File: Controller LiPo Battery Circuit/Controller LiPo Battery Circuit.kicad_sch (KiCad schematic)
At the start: 39 parts, among them CN1 USBA_FEMALE, J1 Jack-DC, Q1 MMUN2133LT1G, Q2 BC548, SW1 ROTARY SW, U1 TPS61090RSAR, U2 MCP73831T-2ACI/OT, X1 TERMBLOCK_1X2, X2 microUSB

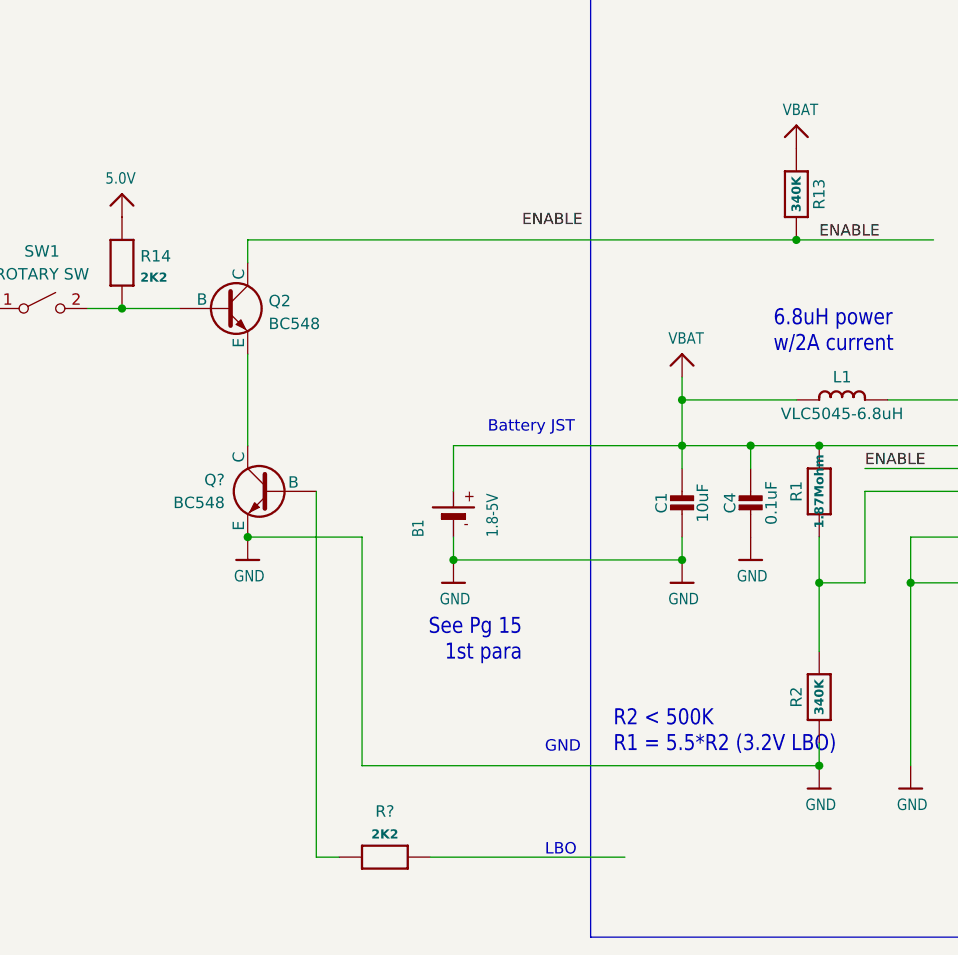
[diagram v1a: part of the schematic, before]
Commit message: Just connected LBO to Enable
Decided that we didn't need transistor control of the LBO to Enable line
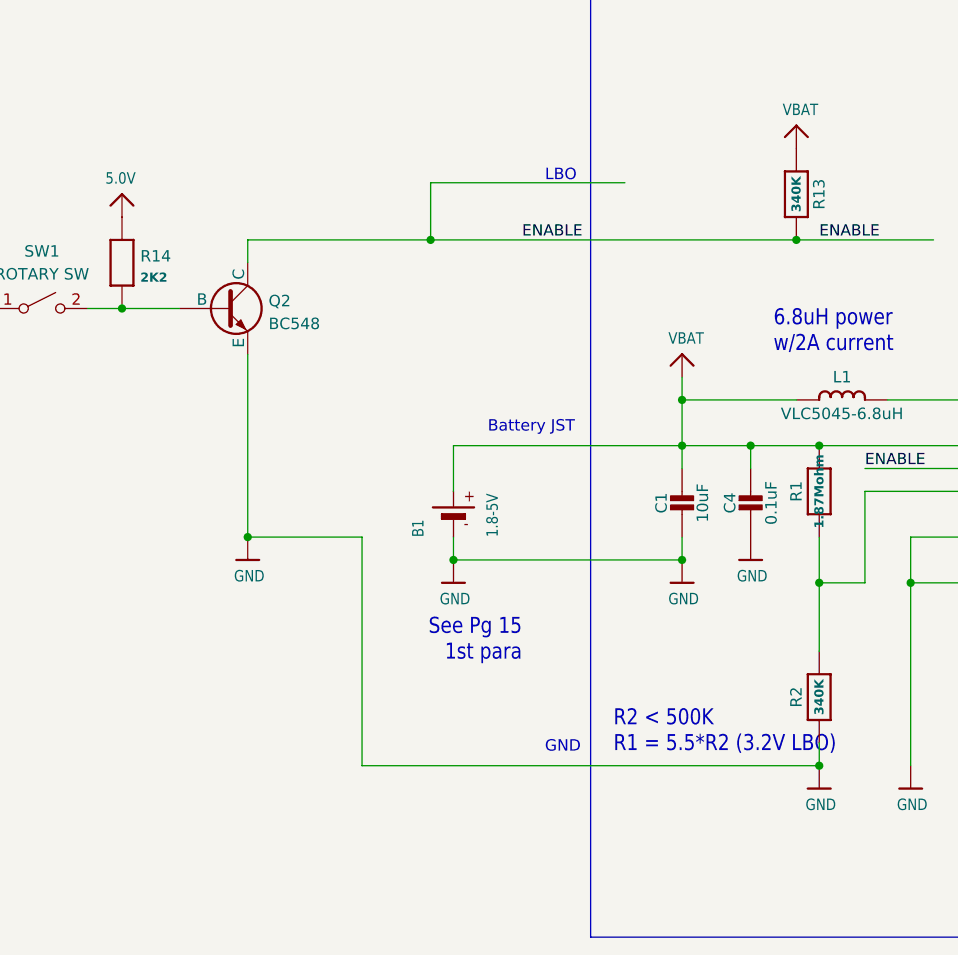
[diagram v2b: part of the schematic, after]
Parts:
- removed Q?: BC548, Package_TO_SOT_THT:TO-92_Inline, symbol Transistor_BJT:BC548
- removed R?: 2K2, Controller LiPo Battery Circuit:0603-MINI, symbol Controller LiPo Battery Circuit-eagle-import:RESISTOR0603MINI
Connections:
- net GND: now also Q2.3 (E)
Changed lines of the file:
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@@
   (junction (at 214.63 111.76) (diameter 0) (color 0 0 0 0)
   )
+  (junction (at 100.33 109.22) (diameter 0) (color 0 0 0 0)
+  )
+  (junction (at 135.89 132.08) (diameter 0) (color 0 0 0 0)
+  )
+  (junction (at 143.51 132.08) (diameter 0) (color 0 0 0 0)
+  )
+  (junction (at 140.97 109.22) (diameter 0) (color 0 0 0 0)
+  )
+  (junction (at 191.77 147.32) (diameter 0) (color 0 0 0 0)
+  )
+  (junction (at 214.63 127) (diameter 0) (color 0 0 0 0)
+  )
+  (junction (at 143.51 147.32) (diameter 0) (color 0 0 0 0)
+  )
+  (junction (at 196.85 127) (diameter 0) (color 0 0 0 0)
+  )
+  (junction (at 260.35 66.04) (diameter 0) (color 0 0 0 0)
+  )
+  (junction (at 270.51 124.46) (diameter 0) (color 0 0 0 0)
+  )
+  (junction (at 270.51 137.16) (diameter 0) (color 0 0 0 0)
+  )
+  (junction (at 336.55 88.9) (diameter 0) (color 0 0 0 0)
+  )
+  (junction (at 267.97 66.04) (diameter 0) (color 0 0 0 0)
+  )
+  (junction (at 143.51 167.64) (diameter 0) (color 0 0 0 0)
+  )
+  (junction (at 273.05 143.51) (diameter 0) (color 0 0 0 0)
+  )
+  (junction (at 128.27 144.78) (diameter 0) (color 0 0 0 0)
+  )
+  (junction (at 191.77 127) (diameter 0) (color 0 0 0 0)
+  )
   (junction (at 80.01 142.24) (diameter 0) (color 0 0 0 0)
   )
-  (junction (at 135.89 132.08) (diameter 0) (color 0 0 0 0)
-  )
-  (junction (at 143.51 132.08) (diameter 0) (color 0 0 0 0)
-  )
-  (junction (at 140.97 109.22) (diameter 0) (color 0 0 0 0)
-  )
-  (junction (at 191.77 147.32) (diameter 0) (color 0 0 0 0)
-  )
-  (junction (at 214.63 127) (diameter 0) (color 0 0 0 0)
-  )
-  (junction (at 143.51 147.32) (diameter 0) (color 0 0 0 0)
-  )
-  (junction (at 196.85 127) (diameter 0) (color 0 0 0 0)
-  )
-  (junction (at 260.35 66.04) (diameter 0) (color 0 0 0 0)
-  )
-  (junction (at 270.51 124.46) (diameter 0) (color 0 0 0 0)
-  )
-  (junction (at 270.51 137.16) (diameter 0) (color 0 0 0 0)
-  )
-  (junction (at 336.55 88.9) (diameter 0) (color 0 0 0 0)
-  )
-  (junction (at 267.97 66.04) (diameter 0) (color 0 0 0 0)
-  )
-  (junction (at 143.51 167.64) (diameter 0) (color 0 0 0 0)
-  )
-  (junction (at 273.05 143.51) (diameter 0) (color 0 0 0 0)
-  )
-  (junction (at 128.27 144.78) (diameter 0) (color 0 0 0 0)
-  )
-  (junction (at 191.77 127) (diameter 0) (color 0 0 0 0)
-  )
   (junction (at 273.05 120.65) (diameter 0) (color 0 0 0 0)
   )
@@
     (stroke (width 0) (type default) (color 0 0 0 0))
   )
+  (wire (pts (xy 100.33 109.22) (xy 140.97 109.22))
+    (stroke (width 0) (type default) (color 0 0 0 0))
+  )
   (wire (pts (xy 102.87 144.78) (xy 128.27 144.78))
     (stroke (width 0) (type default) (color 0 0 0 0))
@@
     (stroke (width 0) (type default) (color 0 0 0 0))
   )
-  (wire (pts (xy 80.01 121.92) (xy 80.01 132.08))
+  (wire (pts (xy 80.01 121.92) (xy 80.01 142.24))
     (stroke (width 0) (type default) (color 0 0 0 0))
   )
@@
     (stroke (width 0) (type default) (color 0 0 0 0))
   )
-  (wire (pts (xy 87.63 137.16) (xy 87.63 177.8))
-    (stroke (width 0) (type default) (color 0 0 0 0))
-  )
   (wire (pts (xy 293.37 78.74) (xy 293.37 71.12))
     (stroke (width 0) (type default) (color 0 0 0 0))
   )
-  (wire (pts (xy 80.01 109.22) (xy 140.97 109.22))
+  (wire (pts (xy 80.01 109.22) (xy 100.33 109.22))
     (stroke (width 0) (type default) (color 0 0 0 0))
   )
@@
     (stroke (width 0) (type default) (color 0 0 0 0))
   )
-  (wire (pts (xy 100.33 177.8) (xy 121.92 177.8))
+  (wire (pts (xy 100.33 102.87) (xy 121.92 102.87))
     (stroke (width 0) (type default) (color 0 0 0 0))
   )
@@
     (stroke (width 0) (type default) (color 0 0 0 0))
   )
+  (wire (pts (xy 100.33 102.87) (xy 100.33 109.22))
+    (stroke (width 0) (type default) (color 0 0 0 0))
+  )
   (wire (pts (xy 148.59 147.32) (xy 148.59 137.16))
     (stroke (width 0) (type default) (color 0 0 0 0))
@@
   )
   (wire (pts (xy 321.31 71.12) (xy 323.85 71.12))
-    (stroke (width 0) (type default) (color 0 0 0 0))
-  )
-  (wire (pts (xy 87.63 177.8) (xy 90.17 177.8))
     (stroke (width 0) (type default) (color 0 0 0 0))
   )
@@
     (effects (font (size 1.27 1.27)) (justify left bottom))
   )
-  (text "LBO\n" (at 113.03 177.8 0)
+  (text "LBO\n" (at 113.03 102.87 0)
     (effects (font (size 1.27 1.27)) (justify left bottom))
   )
@@
     (effects (font (size 1.016 1.016)) (justify right bottom))
   )
-  (label "ENABLE" (at 110.49 107.95 0)
+  (label "ENABLE" (at 110.49 109.22 0)
     (effects (font (size 1.2446 1.2446)) (justify left bottom))
   )
@@
     (pin "E")
   )
-  (symbol (lib_id "Transistor_BJT:BC548") (at 82.55 137.16 0) (mirror y) (unit 1)
-    (in_bom yes) (on_board yes) (fields_autoplaced)
-    (property "Reference" "Q?" (id 0) (at 77.47 135.8899 0)
-      (effects (font (size 1.27 1.27)) (justify left))
-    )
-    (property "Value" "BC548" (id 1) (at 77.47 138.4299 0)
-      (effects (font (size 1.27 1.27)) (justify left))
-    )
-    (property "Footprint" "Package_TO_SOT_THT:TO-92_Inline" (id 2) (at 77.47 139.065 0)
-      (effects (font (size 1.27 1.27) italic) (justify left) hide)
-    )
-    (property "Datasheet" "https://www.onsemi.com/pub/Collateral/BC550-D.pdf" (id 3) (at 82.55 137.16 0)
-      (effects (font (size 1.27 1.27)) (justify left) hide)
-    )
-    (pin "1")
-    (pin "2")
-    (pin "3")
-  )
   (symbol (lib_id "Controller LiPo Battery Circuit-eagle-import:VBAT") (at 140.97 96.52 0) (unit 1)
     (in_bom yes) (on_board yes)
@@
     (pin "1")
   )
-  (symbol (lib_id "Controller LiPo Battery Circuit-eagle-import:RESISTOR0603MINI") (at 95.25 177.8 180) (unit 1)
-    (in_bom yes) (on_board yes) (fields_autoplaced)
-    (property "Reference" "R?" (id 0) (at 95.25 172.72 0))
-    (property "Value" "2K2" (id 1) (at 95.25 175.26 0)
-      (effects (font (size 1.016 1.016) bold))
-    )
-    (property "Footprint" "Controller LiPo Battery Circuit:0603-MINI" (id 2) (at 95.25 177.8 0)
-      (effects (font (size 1.27 1.27)) hide)
-    )
-    (property "Datasheet" "" (id 3) (at 95.25 177.8 0)
-      (effects (font (size 1.27 1.27)) hide)
-    )
-    (pin "1")
-    (pin "2")
-  )
   (symbol (lib_id "Controller LiPo Battery Circuit-eagle-import:RESISTOR0805_NOOUTLINE") (at 191.77 142.24 90) (unit 1)
     (in_bom yes) (on_board yes)
@@
       (reference "Q2") (unit 1) (value "BC548") (footprint "Package_TO_SOT_THT:TO-92_Inline")
     )
-    (path "/2c106d57-d126-491f-b8e5-3d7b48ca676e"
-      (reference "Q?") (unit 1) (value "BC548") (footprint "Package_TO_SOT_THT:TO-92_Inline")
-    )
     (path "/adda07ce-daac-4e4e-9d52-415971c89ae0"
       (reference "R1") (unit 1) (value "1.87Mohm") (footprint "Controller LiPo Battery Circuit:0805-NO")
@@
       (reference "R20") (unit 1) (value "1K") (footprint "Controller LiPo Battery Circuit:0805-NO")
     )
-    (path "/d76d002d-79a6-493d-beee-cfd6c20e9189"
-      (reference "R?") (unit 1) (value "2K2") (footprint "Controller LiPo Battery Circuit:0603-MINI")
-    )
     (path "/1815e0a6-d6ea-443e-92b7-f4945f548a6a"

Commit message: Starting to create PCB
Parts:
- removed X2: microUSB, Controller LiPo Battery Circuit:4UCONN_20329, symbol Controller LiPo Battery Circuit-eagle-import:USBMICRO_20329
- C5: symbol Controller LiPo Battery Circuit-eagle-import:CAP_TANTALUMB/3528_REFLOW -> Controller LiPo Battery Circuit-eagle-import:CAP_TANTALUMB/3528_REFLOW
- J1: symbol Connector:Jack-DC -> Connector:Conn_01x02_Pin
- U2: symbol Controller LiPo Battery Circuit-eagle-import:MCP73831/2 -> Controller LiPo Battery Circuit-eagle-import:MCP73831/2
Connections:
- net 5.0V is gone; now on net +5V: C2.1, C5.+, CN1.VBUS, JP1.6, PWR0.A, R11.2, R14.2, R3.2, R9.2, U1.1 (VOUT), U1.15 (VOUT), U1.16 (VOUT), X1.2
- net +5V: now reaches C6.1, J1.1 (Pin_1), JP2.1, LED3.A, U2.4 (VDD)
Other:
- note added: "Connects to Barrel Jack on HH Controller"
- note removed: "To MicroUSB"
- moved on the sheet: JP2
